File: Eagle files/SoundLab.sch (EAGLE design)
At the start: 138 parts, among them IC1 LM555D, IC2 LM3900D, IC3 LM3900D, IC4 LM324D, IC5 LM555D, IC6 LM386M-1, J7 5.5x2.1mm Barrel, P1 200k, P10 200k, P11 200k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

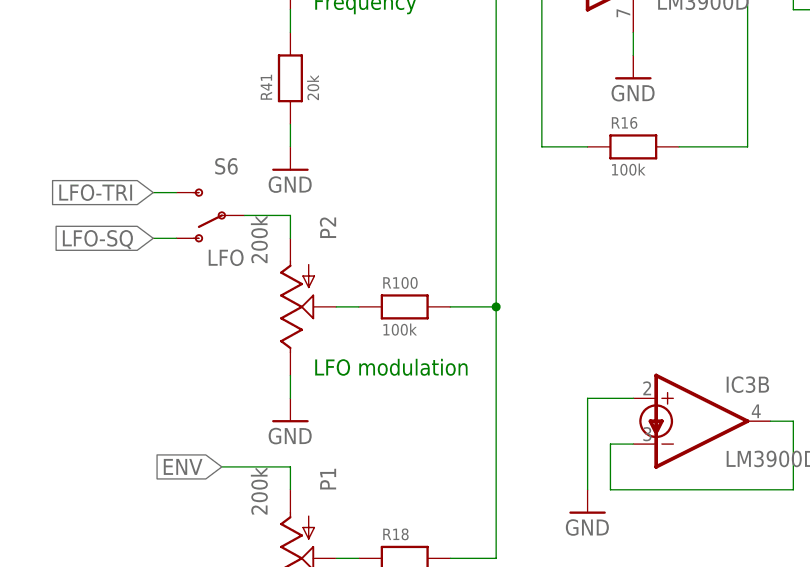
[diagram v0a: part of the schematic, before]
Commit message: R100->R55
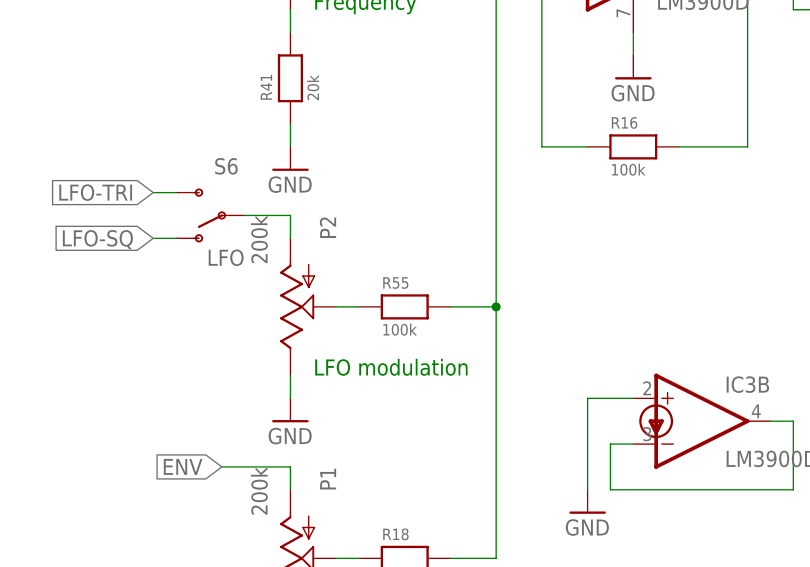
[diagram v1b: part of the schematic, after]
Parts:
- renumbered R100 to R55
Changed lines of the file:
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@@
 <part name="GND3" library="SparkFun" deviceset="GND" device=""/>
 <part name="IC3" library="linear" deviceset="LM3900" device="D"/>
-<part name="R100" library="microbuilder" deviceset="RESISTOR" device="_0805MP" value="100k"/>
+<part name="R55" library="microbuilder" deviceset="RESISTOR" device="_0805MP" value="100k"/>
 <part name="R10" library="microbuilder" deviceset="RESISTOR" device="_0805MP" value="10k"/>
 <part name="R16" library="microbuilder" deviceset="RESISTOR" device="_0805MP" value="100k"/>
@@
 <instance part="IC3" gate="D" x="58.42" y="101.6" rot="MR0"/>
 <instance part="IC3" gate="P" x="-2.54" y="132.08"/>
-<instance part="R100" gate="G$1" x="-27.94" y="93.98"/>
+<instance part="R55" gate="G$1" x="-27.94" y="93.98"/>
 <instance part="R10" gate="G$1" x="38.1" y="101.6"/>
 <instance part="R16" gate="G$1" x="-2.54" y="111.76"/>
@@
 <net name="N$1" class="0">
 <segment>
-<pinref part="R100" gate="G$1" pin="2"/>
+<pinref part="R55" gate="G$1" pin="2"/>
 <wire x1="-17.78" y1="134.62" x2="-17.78" y2="93.98" width="0.1524" layer="91"/>
 <pinref part="R17" gate="G$1" pin="2"/>
@@
 <segment>
 <pinref part="P2" gate="G$1" pin="S"/>
-<pinref part="R100" gate="G$1" pin="1"/>
+<pinref part="R55" gate="G$1" pin="1"/>
 <wire x1="-35.56" y1="93.98" x2="-33.02" y2="93.98" width="0.1524" layer="91"/>
 </segment>
